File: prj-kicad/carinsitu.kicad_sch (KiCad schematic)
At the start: 72 parts, among them P1 BAT, P2 MOT, P3 CONN_3, P4 CONN_4, Q1 TJ15P04M3, SW1 SWITCH_SLIDE, SW2 Reset, U1 LoLin_D1_mini_pro, U2 MIC2860, U3 MAX17044G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

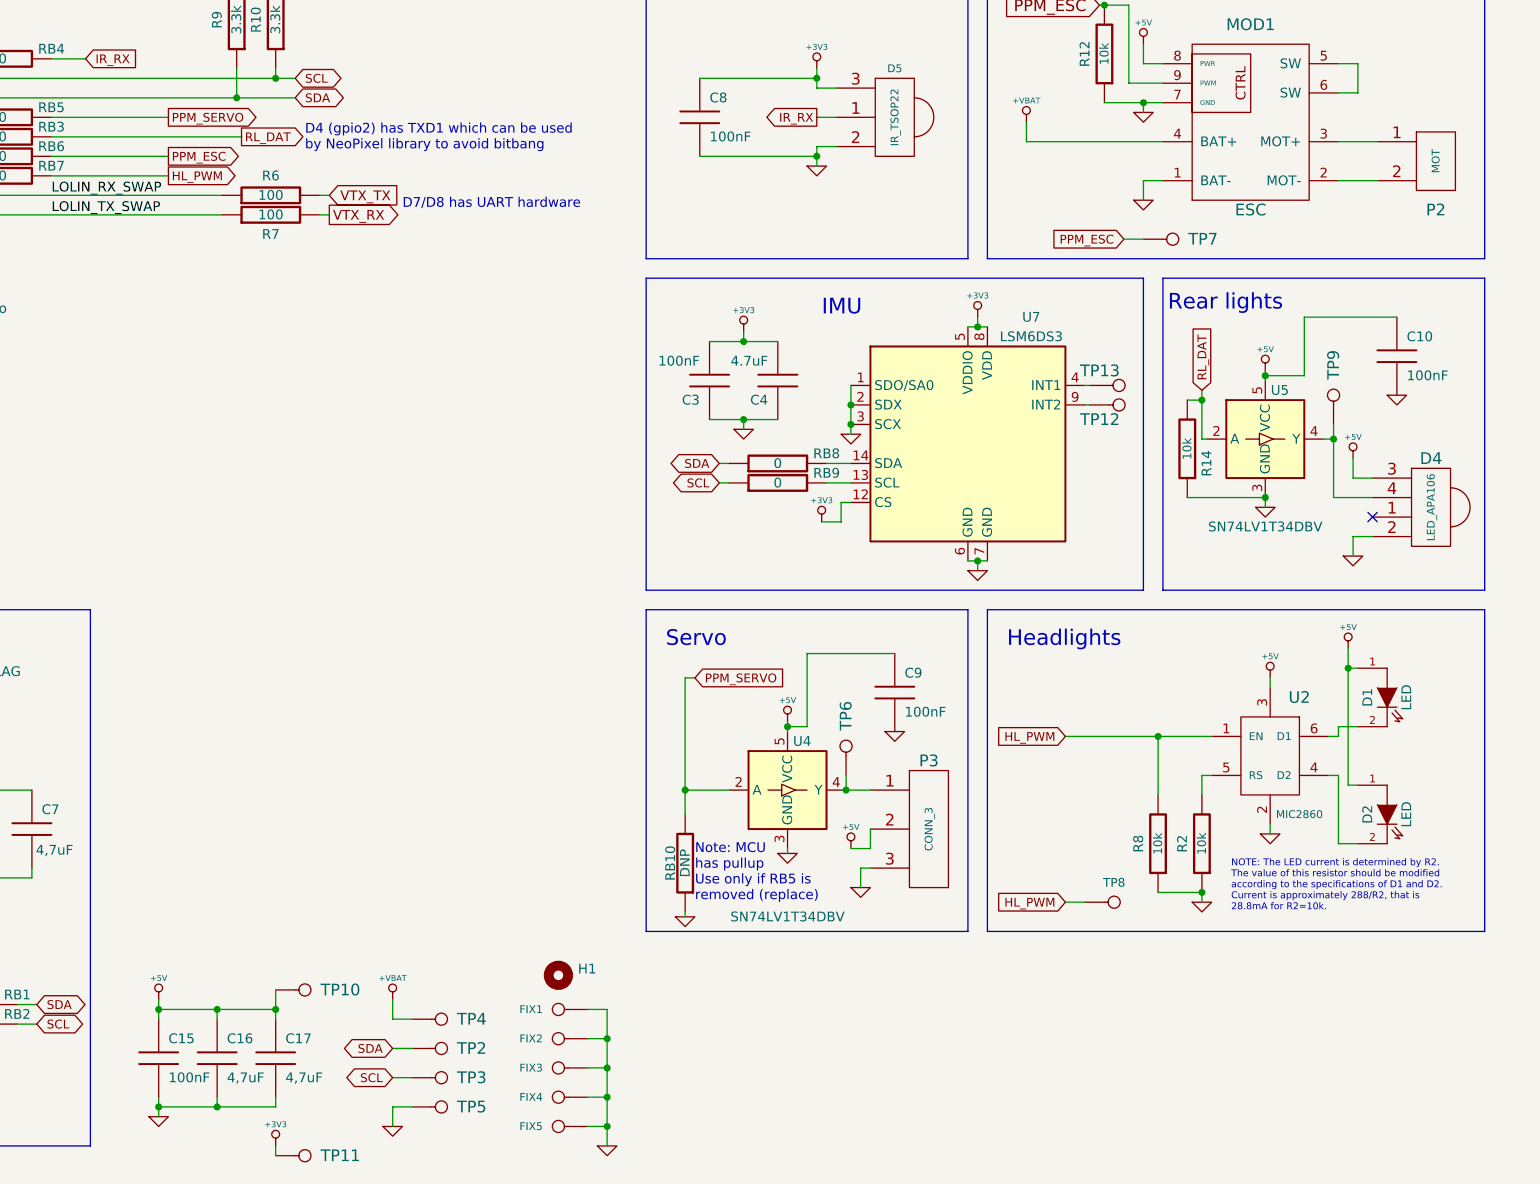
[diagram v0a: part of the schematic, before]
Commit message: Add other decoupling capacitors and route them
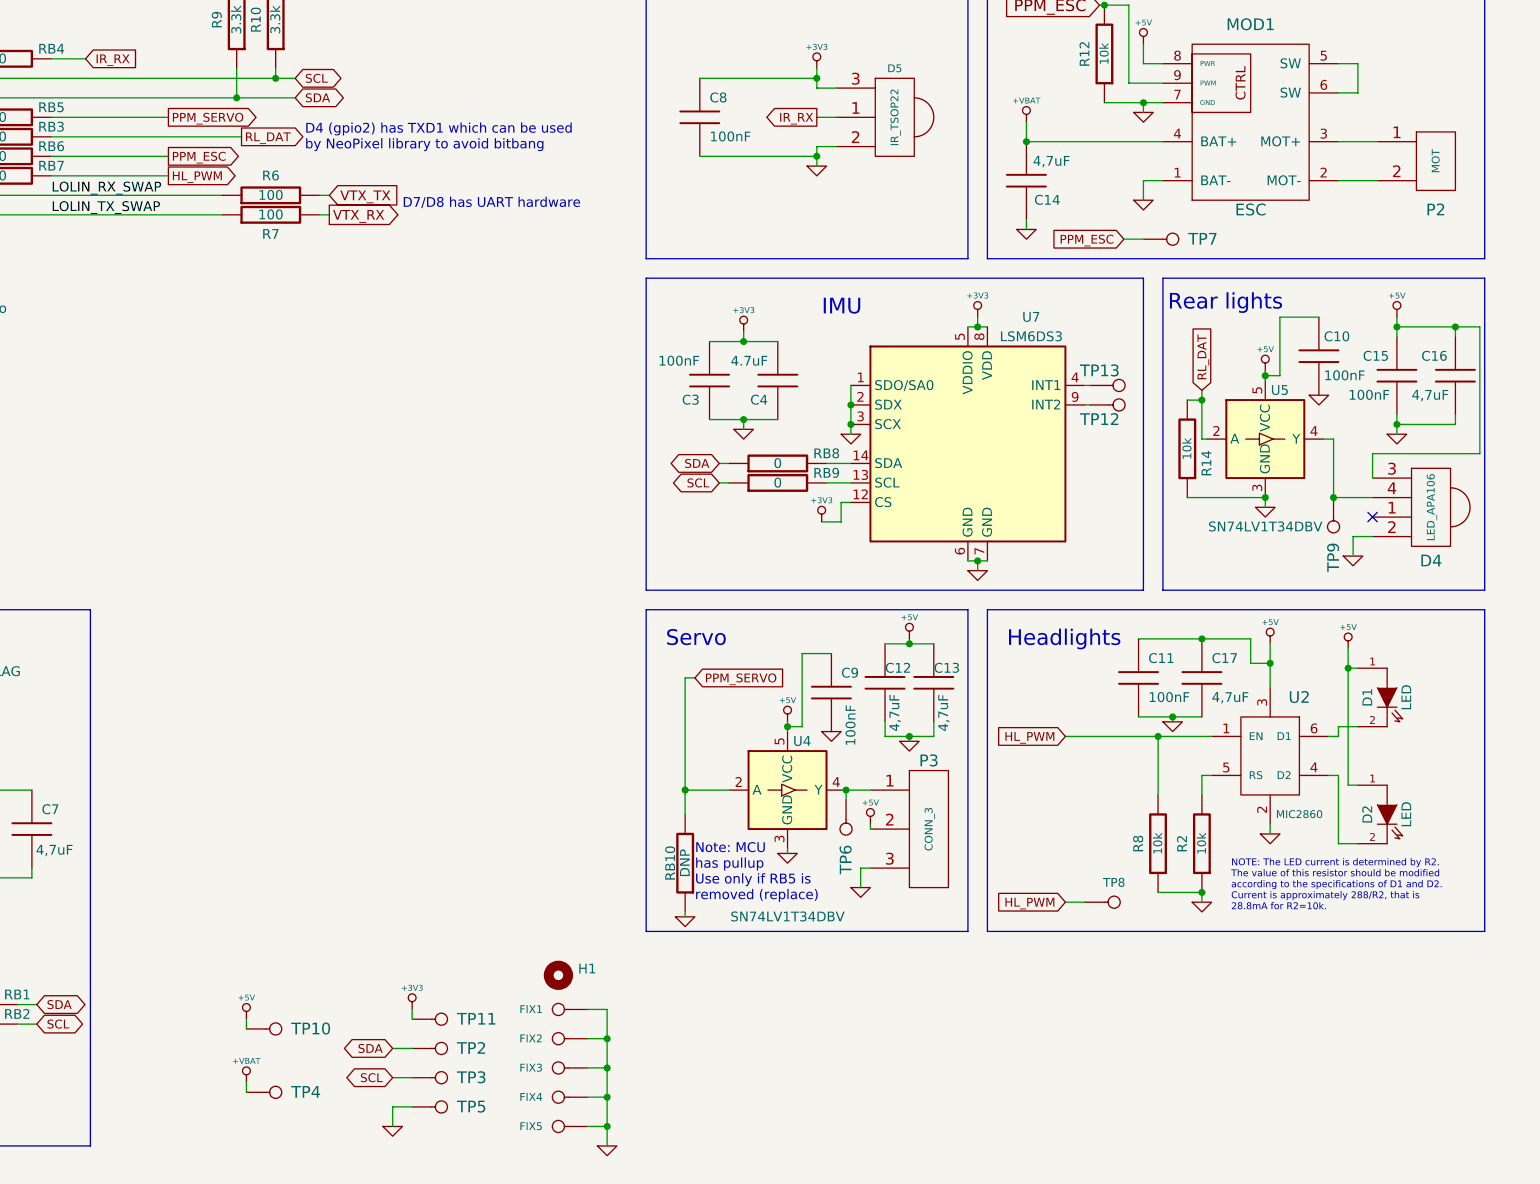
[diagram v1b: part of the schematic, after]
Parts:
- added C11: 100nF, Capacitor_SMD:C_0603_1608Metric, symbol carinsitu:C
- added C12, C13, C14: 4,7uF, Capacitor_SMD:C_0805_2012Metric, symbol carinsitu:C
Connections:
- net +5V: now also C11.1, C12.1, C13.1
- net +VBAT: now also C14.2
- net GND: now also C11.2, C12.2, C13.2, C14.1
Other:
- moved on the sheet: C10, C15, C16, C17, C9, TP10, TP11, TP4, TP6, TP9

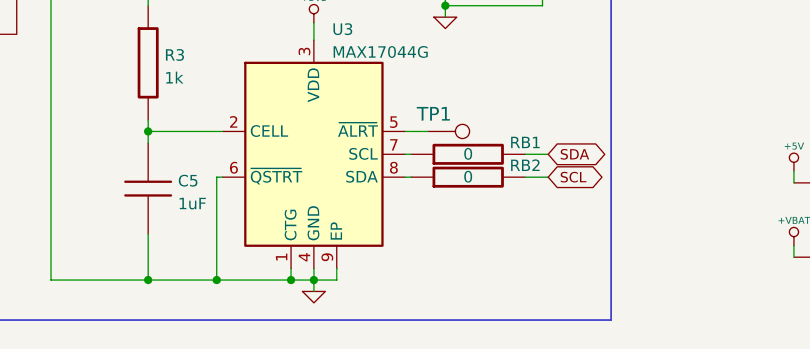
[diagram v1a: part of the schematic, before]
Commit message: Fix GND pin type of ESC
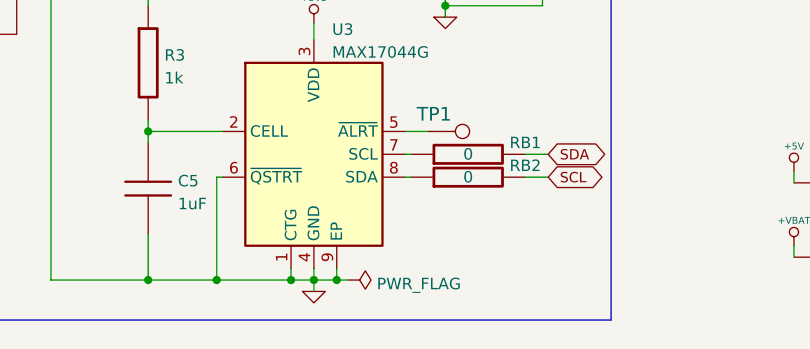
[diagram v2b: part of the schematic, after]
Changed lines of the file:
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@@
   (junction (at 253.365 90.17) (diameter 0) (color 0 0 0 0)
   )
+  (junction (at 69.85 186.055) (diameter 0) (color 0 0 0 0)
+  )
   (junction (at 119.38 53.975) (diameter 0) (color 0 0 0 0)
   )
@@
     (stroke (width 0) (type default) (color 0 0 0 0))
   )
+  (wire (pts (xy 69.85 186.055) (xy 71.12 186.055))
+    (stroke (width 0) (type default) (color 0 0 0 0))
+  )
   (wire (pts (xy 203.835 137.16) (xy 207.01 137.16))
     (stroke (width 0) (type default) (color 0 0 0 0))
@@
     (pin "5")
   )
+  (symbol (lib_id "power:PWR_FLAG") (at 71.12 186.055 270) (unit 1)
+    (in_bom yes) (on_board yes) (fields_autoplaced)
+    (property "Reference" "#FLG01" (id 0) (at 73.025 186.055 0)
+      (effects (font (size 1.27 1.27)) hide)
+    )
+    (property "Value" "PWR_FLAG" (id 1) (at 74.295 186.4888 90)
+      (effects (font (size 1.27 1.27)) (justify left))
+    )
+    (property "Footprint" "" (id 2) (at 71.12 186.055 0)
+      (effects (font (size 1.27 1.27)) hide)
+    )
+    (property "Datasheet" "~" (id 3) (at 71.12 186.055 0)
+      (effects (font (size 1.27 1.27)) hide)
+    )
+    (pin "1")
+  )
   (symbol (lib_id "carinsitu:GND") (at 222.25 71.12 0) (unit 1)
     (in_bom yes) (on_board yes)
@@
   )
   (symbol_instances
+    (path "/172b8e6b-715e-4a39-b803-982f7a1cef45"
+      (reference "#FLG01") (unit 1) (value "PWR_FLAG") (footprint "")
+    )
     (path "/72432868-7bcd-4a68-adb7-1800ac178c45"
       (reference "#FLG0101") (unit 1) (value "PWR_FLAG") (footprint "")

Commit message: Add TVS diode protection
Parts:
- added D3: SMAJ12CA, Diode_SMD:D_SMA, symbol Device:D_TVS
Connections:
- net GND: now also D3.1 (A1)
- net at F1.2, Q1.2 (D): now also D3.2 (A2)
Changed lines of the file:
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@@
   (junction (at 121.92 37.465) (diameter 0) (color 0 0 0 0)
   )
+  (junction (at 38.1 142.24) (diameter 0) (color 0 0 0 0)
+  )
   (junction (at 245.11 124.46) (diameter 0) (color 0 0 0 0)
   )
@@
   (junction (at 253.365 90.17) (diameter 0) (color 0 0 0 0)
   )
+  (junction (at 62.865 130.81) (diameter 0) (color 0 0 0 0)
+  )
   (junction (at 69.85 186.055) (diameter 0) (color 0 0 0 0)
   )
@@
     (stroke (width 0) (type default) (color 0 0 0 0))
   )
+  (wire (pts (xy 62.865 136.525) (xy 62.865 130.81))
+    (stroke (width 0) (type default) (color 0 0 0 0))
+  )
   (wire (pts (xy 38.1 186.055) (xy 48.895 186.055))
     (stroke (width 0) (type default) (color 0 0 0 0))
@@
     (stroke (width 0) (type default) (color 0 0 0 0))
   )
+  (wire (pts (xy 62.865 130.81) (xy 65.405 130.81))
+    (stroke (width 0) (type default) (color 0 0 0 0))
+  )
   (wire (pts (xy 207.01 137.16) (xy 210.185 137.16))
     (stroke (width 0) (type default) (color 0 0 0 0))
@@
     (stroke (width 0) (type default) (color 0 0 0 0))
   )
+  (wire (pts (xy 38.1 136.525) (xy 38.1 142.24))
+    (stroke (width 0) (type default) (color 0 0 0 0))
+  )
   (wire (pts (xy 73.66 34.925) (xy 73.66 38.735))
     (stroke (width 0) (type default) (color 0 0 0 0))
@@
     (stroke (width 0) (type default) (color 0 0 0 0))
   )
-  (wire (pts (xy 61.595 130.81) (xy 65.405 130.81))
+  (wire (pts (xy 61.595 130.81) (xy 62.865 130.81))
     (stroke (width 0) (type default) (color 0 0 0 0))
   )
@@
     (stroke (width 0) (type default) (color 0 0 0 0))
   )
+  (wire (pts (xy 58.42 136.525) (xy 62.865 136.525))
+    (stroke (width 0) (type default) (color 0 0 0 0))
+  )
   (wire (pts (xy 260.985 98.425) (xy 262.255 98.425))
     (stroke (width 0) (type default) (color 0 0 0 0))
@@
     (stroke (width 0) (type default) (color 0 0 0 0))
   )
+  (wire (pts (xy 50.8 136.525) (xy 38.1 136.525))
+    (stroke (width 0) (type default) (color 0 0 0 0))
+  )
   (wire (pts (xy 90.805 174.625) (xy 93.345 174.625))
     (stroke (width 0) (type default) (color 0 0 0 0))
@@
     (pin "1")
   )
+  (symbol (lib_id "Device:D_TVS") (at 54.61 136.525 0) (unit 1)
+    (in_bom yes) (on_board yes)
+    (property "Reference" "D3" (id 0) (at 54.61 139.065 0))
+    (property "Value" "SMAJ12CA" (id 1) (at 54.61 134.0921 0))
+    (property "Footprint" "Diode_SMD:D_SMA" (id 2) (at 54.61 136.525 0)
+      (effects (font (size 1.27 1.27)) hide)
+    )
+    (property "Datasheet" "~" (id 3) (at 54.61 136.525 0)
+      (effects (font (size 1.27 1.27)) hide)
+    )
+    (pin "1")
+    (pin "2")
+  )
   (symbol (lib_id "carinsitu:R") (at 124.46 43.815 180) (unit 1)
     (in_bom yes) (on_board yes)
@@
   (symbol (lib_id "carinsitu:R") (at 54.61 142.24 90) (unit 1)
     (in_bom yes) (on_board yes)
-    (property "Reference" "R4" (id 0) (at 54.61 139.7 90))
+    (property "Reference" "R4" (id 0) (at 54.61 144.78 90))
     (property "Value" "1k" (id 1) (at 54.61 142.24 90))
     (property "Footprint" "Resistor_SMD:R_0805_2012Metric" (id 2) (at 54.61 142.24 0)
@@
       (reference "D2") (unit 1) (value "LED") (footprint "LED_THT:LED_D5.0mm_Horizontal_O3.81mm_Z3.0mm")
     )
+    (path "/a2ae2c5e-3eba-4997-8dbf-3d43591e8528"
+      (reference "D3") (unit 1) (value "SMAJ12CA") (footprint "Diode_SMD:D_SMA")
+    )
     (path "/00000000-0000-0000-0000-00005d24ade3"

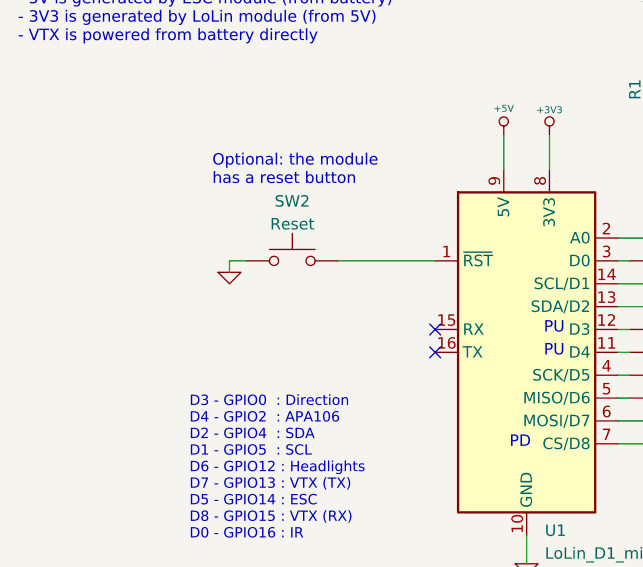
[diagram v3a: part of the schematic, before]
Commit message: Add reset capacitor
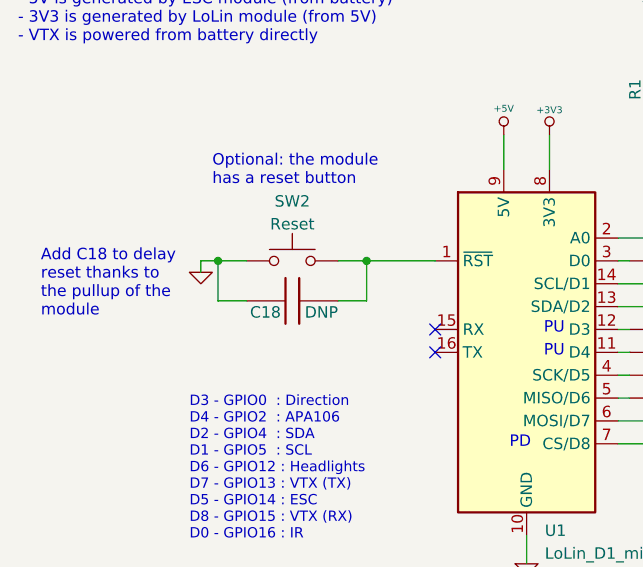
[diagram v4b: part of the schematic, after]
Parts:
- added C18: DNP, Capacitor_SMD:C_0805_2012Metric, symbol carinsitu:C
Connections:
- net GND: now also C18.1
- net at SW2.2, U1.1 (~{RST}): now also C18.2
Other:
- note added: "Add C18 to delay reset thanks to the pullup of the module"
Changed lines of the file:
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@@
   (junction (at 247.015 19.05) (diameter 0) (color 0 0 0 0)
   )
+  (junction (at 53.34 48.895) (diameter 0) (color 0 0 0 0)
+  )
   (junction (at 121.92 37.465) (diameter 0) (color 0 0 0 0)
   )
@@
   (junction (at 231.775 29.21) (diameter 0) (color 0 0 0 0)
   )
+  (junction (at 36.83 48.895) (diameter 0) (color 0 0 0 0)
+  )
   (junction (at 185.42 85.725) (diameter 0) (color 0 0 0 0)
   )
@@
     (stroke (width 0) (type default) (color 0 0 0 0))
   )
+  (wire (pts (xy 53.34 48.895) (xy 60.96 48.895))
+    (stroke (width 0) (type default) (color 0 0 0 0))
+  )
   (wire (pts (xy 67.31 186.055) (xy 69.85 186.055))
     (stroke (width 0) (type default) (color 0 0 0 0))
@@
     (stroke (width 0) (type default) (color 0 0 0 0))
   )
+  (wire (pts (xy 36.83 48.895) (xy 40.005 48.895))
+    (stroke (width 0) (type default) (color 0 0 0 0))
+  )
   (wire (pts (xy 77.47 169.545) (xy 80.01 169.545))
     (stroke (width 0) (type default) (color 0 0 0 0))
@@
     (stroke (width 0) (type default) (color 0 0 0 0))
   )
-  (wire (pts (xy 38.1 48.895) (xy 38.1 50.165))
+  (wire (pts (xy 34.925 48.895) (xy 34.925 50.165))
     (stroke (width 0) (type default) (color 0 0 0 0))
   )
@@
     (stroke (width 0) (type default) (color 0 0 0 0))
   )
+  (wire (pts (xy 40.005 53.34) (xy 36.83 53.34))
+    (stroke (width 0) (type default) (color 0 0 0 0))
+  )
   (wire (pts (xy 250.19 17.78) (xy 252.095 17.78))
     (stroke (width 0) (type default) (color 0 0 0 0))
@@
     (stroke (width 0) (type default) (color 0 0 0 0))
   )
-  (wire (pts (xy 40.005 48.895) (xy 38.1 48.895))
+  (wire (pts (xy 36.83 48.895) (xy 34.925 48.895))
     (stroke (width 0) (type default) (color 0 0 0 0))
   )
@@
     (stroke (width 0) (type default) (color 0 0 0 0))
   )
+  (wire (pts (xy 53.34 53.34) (xy 53.34 48.895))
+    (stroke (width 0) (type default) (color 0 0 0 0))
+  )
   (wire (pts (xy 239.395 137.16) (xy 239.395 144.78))
     (stroke (width 0) (type default) (color 0 0 0 0))
@@
     (stroke (width 0) (type default) (color 0 0 0 0))
   )
-  (wire (pts (xy 50.165 48.895) (xy 60.96 48.895))
+  (wire (pts (xy 50.165 48.895) (xy 53.34 48.895))
     (stroke (width 0) (type default) (color 0 0 0 0))
   )
@@
     (stroke (width 0) (type default) (color 0 0 0 0))
   )
+  (wire (pts (xy 36.83 53.34) (xy 36.83 48.895))
+    (stroke (width 0) (type default) (color 0 0 0 0))
+  )
   (wire (pts (xy 194.945 56.515) (xy 197.485 56.515))
     (stroke (width 0) (type default) (color 0 0 0 0))
@@
     (stroke (width 0) (type default) (color 0 0 0 0))
   )
+  (wire (pts (xy 50.165 53.34) (xy 53.34 53.34))
+    (stroke (width 0) (type default) (color 0 0 0 0))
+  )
   (wire (pts (xy 237.49 46.99) (xy 237.49 49.53))
     (stroke (width 0) (type default) (color 0 0 0 0))
@@
     (effects (font (size 1.27 1.27)) (justify left bottom))
   )
+  (text "Add C18 to delay\nreset thanks to\nthe pullup of the\nmodule"
+    (at 17.145 55.245 0)
+    (effects (font (size 1.27 1.27)) (justify left bottom))
+  )
   (text "Rear lights" (at 240.665 81.915 0)
     (effects (font (size 2.032 2.032)) (justify left bottom))
@@
     (pin "2")
   )
+  (symbol (lib_id "carinsitu:C") (at 45.085 53.34 90) (unit 1)
+    (in_bom yes) (on_board yes)
+    (property "Reference" "C18" (id 0) (at 43.815 54.61 90)
+      (effects (font (size 1.27 1.27)) (justify left))
+    )
+    (property "Value" "DNP" (id 1) (at 50.165 54.61 90)
+      (effects (font (size 1.27 1.27)) (justify left))
+    )
+    (property "Footprint" "Capacitor_SMD:C_0805_2012Metric" (id 2) (at 45.085 53.34 0)
+      (effects (font (size 1.524 1.524)) hide)
+    )
+    (property "Datasheet" "" (id 3) (at 45.085 53.34 0)
+      (effects (font (size 1.524 1.524)))
+    )
+    (pin "1")
+    (pin "2")
+  )
   (symbol (lib_id "carinsitu:C") (at 48.895 175.895 0) (unit 1)
     (in_bom yes) (on_board yes) (fields_autoplaced)
@@
     (pin "1")
   )
-  (symbol (lib_id "carinsitu:GND") (at 38.1 50.165 0) (unit 1)
+  (symbol (lib_id "carinsitu:GND") (at 34.925 50.165 0) (unit 1)
     (in_bom yes) (on_board yes) (fields_autoplaced)
-    (property "Reference" "#PWR011" (id 0) (at 38.1 50.165 0)
+    (property "Reference" "#PWR011" (id 0) (at 34.925 50.165 0)
       (effects (font (size 0.762 0.762)) hide)
     )
-    (property "Value" "GND" (id 1) (at 38.1 51.943 0)
+    (property "Value" "GND" (id 1) (at 34.925 51.943 0)
       (effects (font (size 0.762 0.762)) hide)
     )
-    (property "Footprint" "" (id 2) (at 38.1 50.165 0)
+    (property "Footprint" "" (id 2) (at 34.925 50.165 0)
       (effects (font (size 1.524 1.524)))
     )
-    (property "Datasheet" "" (id 3) (at 38.1 50.165 0)
+    (property "Datasheet" "" (id 3) (at 34.925 50.165 0)
       (effects (font (size 1.524 1.524)))
     )
@@
       (reference "C17") (unit 1) (value "4,7uF") (footprint "Capacitor_SMD:C_0805_2012Metric")
     )
+    (path "/4b04131a-365d-419a-84c1-f43ff8a09c65"
+      (reference "C18") (unit 1) (value "DNP") (footprint "Capacitor_SMD:C_0805_2012Metric")
+    )
     (path "/00000000-0000-0000-0000-00005d132ea5"
